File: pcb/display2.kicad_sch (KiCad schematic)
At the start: 35 parts, among them Q13 2N7002K, Q14 2N7002K, Q15 2N7002K, Q16 2N7002K, Q17 BSS84, Q18 BSS84, Q19 BSS84, Q20 BSS84, Q21 BSS84, Q22 BSS84, Q23 BSS84, Q24 BSS84, U3 74HC595

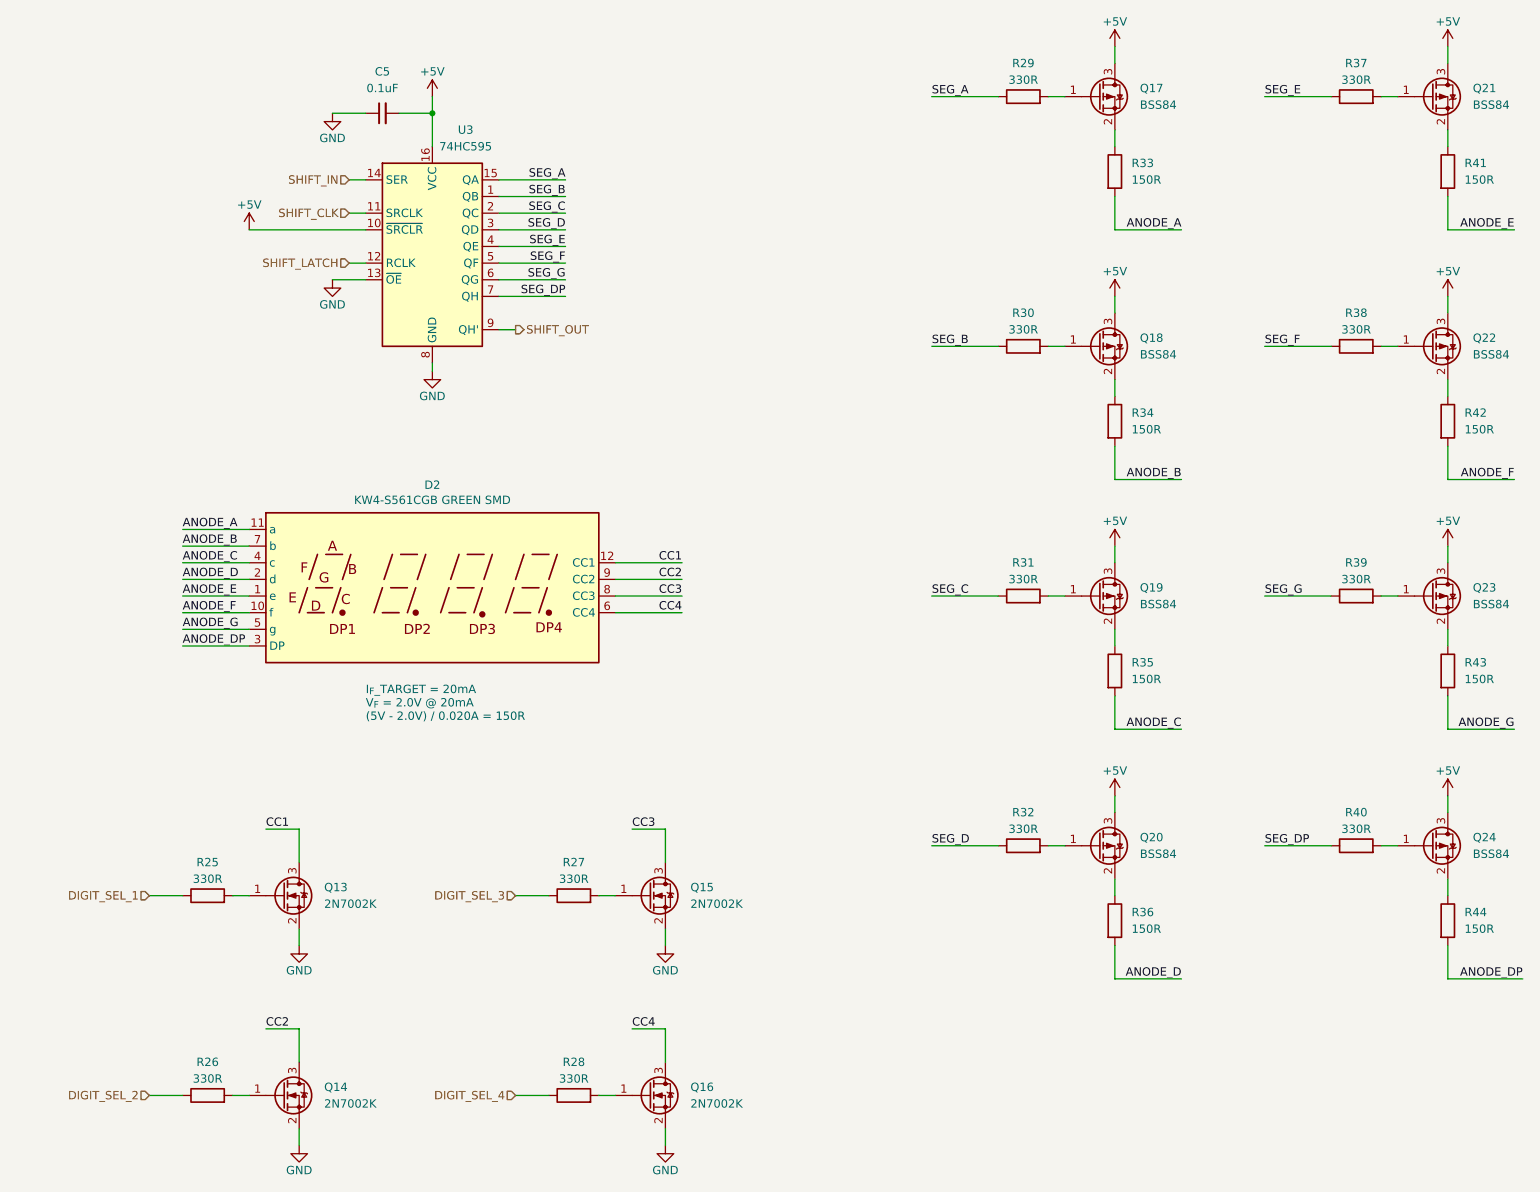
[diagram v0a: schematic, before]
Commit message: tentative schematic for common cathode
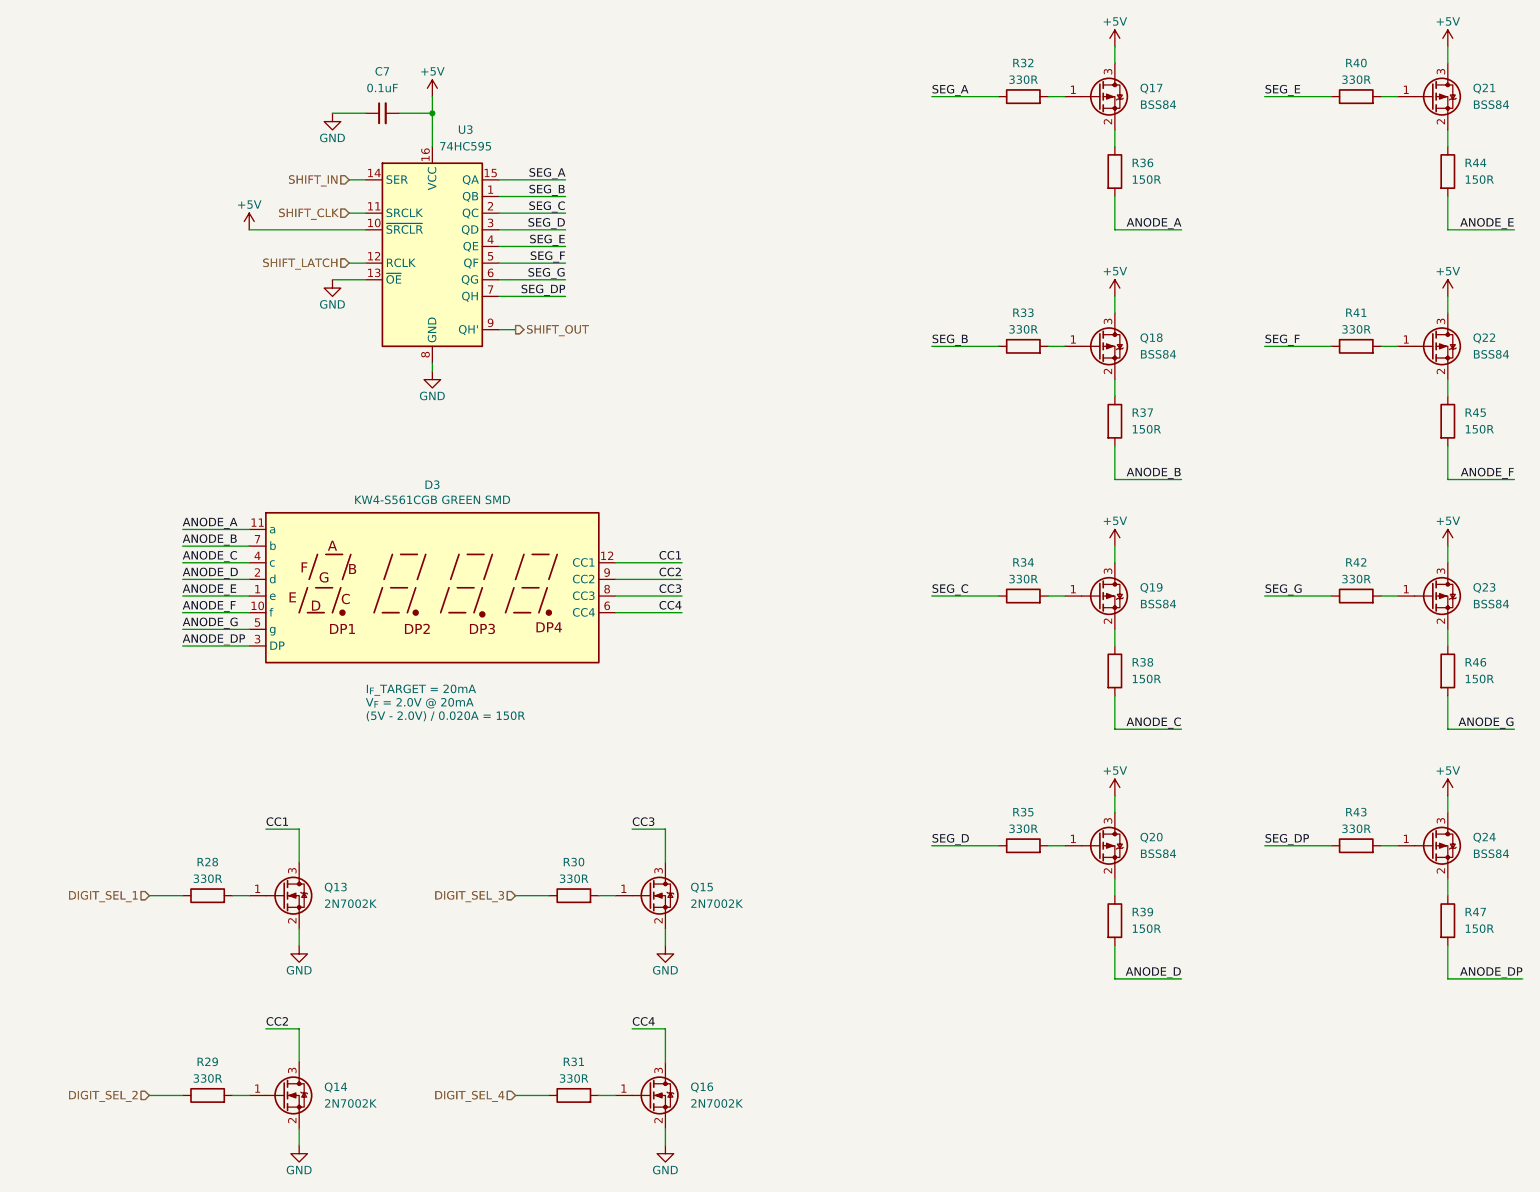
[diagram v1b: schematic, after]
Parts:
- C7: renamed from C5; footprint (none) -> Capacitor_SMD:C_0805_2012Metric_Pad1.18x1.45mm_HandSolder
- R28: renamed from R25; footprint Resistor_SMD:R_0805_2012Metric_Pad1.15x1.40mm_HandSolder -> Resistor_SMD:R_0805_2012Metric_Pad1.20x1.40mm_HandSolder
- R29: renamed from R26; footprint Resistor_SMD:R_0805_2012Metric_Pad1.15x1.40mm_HandSolder -> Resistor_SMD:R_0805_2012Metric_Pad1.20x1.40mm_HandSolder
- R30: renamed from R27; footprint Resistor_SMD:R_0805_2012Metric_Pad1.15x1.40mm_HandSolder -> Resistor_SMD:R_0805_2012Metric_Pad1.20x1.40mm_HandSolder
- R31: renamed from R28; footprint Resistor_SMD:R_0805_2012Metric_Pad1.15x1.40mm_HandSolder -> Resistor_SMD:R_0805_2012Metric_Pad1.20x1.40mm_HandSolder
- R32: renamed from R29; footprint Resistor_SMD:R_0805_2012Metric_Pad1.15x1.40mm_HandSolder -> Resistor_SMD:R_0805_2012Metric_Pad1.20x1.40mm_HandSolder
- R33: renamed from R30; footprint Resistor_SMD:R_0805_2012Metric_Pad1.15x1.40mm_HandSolder -> Resistor_SMD:R_0805_2012Metric_Pad1.20x1.40mm_HandSolder
- R34: renamed from R31; footprint Resistor_SMD:R_0805_2012Metric_Pad1.15x1.40mm_HandSolder -> Resistor_SMD:R_0805_2012Metric_Pad1.20x1.40mm_HandSolder
- R35: renamed from R32; footprint Resistor_SMD:R_0805_2012Metric_Pad1.15x1.40mm_HandSolder -> Resistor_SMD:R_0805_2012Metric_Pad1.20x1.40mm_HandSolder
- R36: renamed from R33; footprint (none) -> Resistor_SMD:R_0805_2012Metric_Pad1.20x1.40mm_HandSolder
- R37: renamed from R34; footprint (none) -> Resistor_SMD:R_0805_2012Metric_Pad1.20x1.40mm_HandSolder
- R38: renamed from R35; footprint (none) -> Resistor_SMD:R_0805_2012Metric_Pad1.20x1.40mm_HandSolder
- R39: renamed from R36; footprint (none) -> Resistor_SMD:R_0805_2012Metric_Pad1.20x1.40mm_HandSolder
- R40: renamed from R37; footprint Resistor_SMD:R_0805_2012Metric_Pad1.15x1.40mm_HandSolder -> Resistor_SMD:R_0805_2012Metric_Pad1.20x1.40mm_HandSolder
- R41: renamed from R38; footprint Resistor_SMD:R_0805_2012Metric_Pad1.15x1.40mm_HandSolder -> Resistor_SMD:R_0805_2012Metric_Pad1.20x1.40mm_HandSolder
- R42: renamed from R39; footprint Resistor_SMD:R_0805_2012Metric_Pad1.15x1.40mm_HandSolder -> Resistor_SMD:R_0805_2012Metric_Pad1.20x1.40mm_HandSolder
- R43: renamed from R40; footprint Resistor_SMD:R_0805_2012Metric_Pad1.15x1.40mm_HandSolder -> Resistor_SMD:R_0805_2012Metric_Pad1.20x1.40mm_HandSolder
- R44: renamed from R41; footprint (none) -> Resistor_SMD:R_0805_2012Metric_Pad1.20x1.40mm_HandSolder
- R45: renamed from R42; footprint (none) -> Resistor_SMD:R_0805_2012Metric_Pad1.20x1.40mm_HandSolder
- R46: renamed from R43; footprint (none) -> Resistor_SMD:R_0805_2012Metric_Pad1.20x1.40mm_HandSolder
- R47: renamed from R44; footprint (none) -> Resistor_SMD:R_0805_2012Metric_Pad1.20x1.40mm_HandSolder
- renumbered D2 to D3

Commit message: common anode schematic
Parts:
- removed C7: 0.1uF, Capacitor_SMD:C_0805_2012Metric_Pad1.18x1.45mm_HandSolder, symbol Device:C_Small
- removed D3: KW4-S561CGB GREEN SMD, mtg_life_counter:KW4-S561xxB_SMD, symbol mtg_life_counter:KW4-S561CxB
- removed Q13, Q14, Q15, Q16: 2N7002K, Package_TO_SOT_SMD:SOT-23, symbol Transistor_FET:2N7002K
- removed Q17, Q18, Q19, Q20, Q21, Q22, Q23, Q24: BSS84, Package_TO_SOT_SMD:SOT-23, symbol Transistor_FET:BSS84
- removed R34, R35, R40, R41, R42, R43: 330R, Resistor_SMD:R_0805_2012Metric_Pad1.20x1.40mm_HandSolder, symbol Device:R
- removed R36, R37, R38, R39, R44, R45, R46, R47: 150R, Resistor_SMD:R_0805_2012Metric_Pad1.20x1.40mm_HandSolder, symbol Device:R
- removed U3: 74HC595, Package_SO:SOIC-16_3.9x9.9mm_P1.27mm, symbol 74xx:74HC595
- added D3: KW4-S561AGB, mtg_life_counter:KW4-S561xxB_SMD, symbol mtg_life_counter:KW4-S561AxB
- added Q5, Q6, Q7, Q8: DMG2301L, Package_TO_SOT_SMD:SOT-23, symbol Transistor_FET:DMG2301L
- added R21, R22, R23, R24: 330R, Resistor_SMD:R_0805_2012Metric_Pad1.20x1.40mm_HandSolder, symbol Device:R
- added R25, R26, R27: 150R, Resistor_SMD:R_0805_2012Metric_Pad1.20x1.40mm_HandSolder, symbol Device:R
- added U3: TPIC6C596, Package_SO:SOIC-16_3.9x9.9mm_P1.27mm, symbol mtg_life_counter:TPIC6C596
- R28, R29, R30, R31, R32: value 330R -> 150R
- R33: value 330R -> 10k
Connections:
- net SEG_B is gone; now on net +5V: R33.1
- net +5V: now also Q5.3 (D), Q6.3 (D), Q7.3 (D), Q8.3 (D), U3.1 (VCC)
- net DIGIT_SEL_1: now also R21.1; no longer R28.1
- net DIGIT_SEL_2: now also R22.1; no longer R29.1
- net DIGIT_SEL_3: now also R23.1; no longer R30.1
- net DIGIT_SEL_4: now also R24.1; no longer R31.1
- net GND: now also U3.16 (GND), U3.8 (~{G})
- net SHIFT_CLK: now also U3.15 (SRCK)
- net SHIFT_IN: now also U3.2 (SER_IN)
- net SHIFT_LATCH: now also U3.10 (RCLK)
- net SHIFT_OUT: now also U3.9 (SER_OUT)
- net at R33.2: now also U3.7 (~{SRCLR})
- net SF: now reaches R30.2
- net SF: now also U3.12 (DRAIN5)
- net SE: now reaches R29.2
- net SE: now also U3.11 (DRAIN4)
- net SD: now reaches R28.2
- net SD: now also U3.6 (DRAIN3)
- net SG: now reaches R31.2
- net SG: now also U3.13 (DRAIN6)
- net SDP: now reaches R32.2
- net SDP: now also U3.14 (DRAIN7)
- net SEG_A renamed ADP
- net ADP: now also D3.3 (DP)
- new net: Q7.1 (G), R23.2
- new net: Q8.1 (G), R24.2
- new net: Q5.1 (G), R21.2
- new net: Q6.1 (G), R22.2
- new net AA: D3.11 (a), R25.1
- new net AB: D3.7 (b), R26.1
- new net AC: D3.4 (c), R27.1
- new net AD: D3.2 (d), R28.1
- new net AE: D3.1 (e), R29.1
- new net AF: D3.10 (f), R30.1
- new net AG: D3.5 (g), R31.1
- new net CA1: D3.12 (CA1), Q5.2 (S)
- new net CA2: D3.9 (CA2), Q6.2 (S)
- new net CA3: D3.8 (CA3), Q7.2 (S)
- new net CA4: D3.6 (CA4), Q8.2 (S)
- new net SA: R25.2, U3.3 (DRAIN0)
- new net SB: R26.2, U3.4 (DRAIN1)
- new net SC: R27.2, U3.5 (DRAIN2)

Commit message: continue wip
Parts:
- added C6: 0.1uF, Capacitor_SMD:C_0805_2012Metric_Pad1.18x1.45mm_HandSolder, symbol Device:C_Small
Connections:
- net +5V: now also C6.1
- net GND: now also C6.2
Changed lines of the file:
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@@
+	(wire
+		(pts
+			(xy 198.12 48.26) (xy 198.12 50.8)
+		)
+		(stroke
+			(width 0)
+			(type default)
+		)
+	)
 	(wire
 		(pts
@@
 		(pts
 			(xy 63.5 73.66) (xy 90.17 73.66)
+		)
+		(stroke
+			(width 0)
+			(type default)
+		)
+	)
+	(wire
+		(pts
+			(xy 198.12 55.88) (xy 198.12 58.42)
 		)
 		(stroke
@@
 	)
 	(symbol
+		(lib_id "power:GND")
+		(at 198.12 58.42 0)
+		(unit 1)
+		(exclude_from_sim no)
+		(in_bom yes)
+		(on_board yes)
+		(dnp no)
+		(property "Reference" "#PWR063"
+			(at 198.12 64.77 0)
+			(effects
+				(font
+					(size 1.27 1.27)
+				)
+				(hide yes)
+			)
+		)
+		(property "Value" "GND"
+			(at 198.12 62.23 0)
+			(effects
+				(font
+					(size 1.27 1.27)
+				)
+			)
+		)
+		(property "Footprint" ""
+			(at 198.12 58.42 0)
+			(effects
+				(font
+					(size 1.27 1.27)
+				)
+				(hide yes)
+			)
+		)
+		(property "Datasheet" ""
+			(at 198.12 58.42 0)
+			(effects
+				(font
+					(size 1.27 1.27)
+				)
+				(hide yes)
+			)
+		)
+		(property "Description" "Power symbol creates a global label with name \"GND\" , ground"
+			(at 198.12 58.42 0)
+			(effects
+				(font
+					(size 1.27 1.27)
+				)
+				(hide yes)
+			)
+		)
+		(pin "1"
+		)
+		(instances
+			(project "mtg_life_counter"
+				(path "/1883df74-0bd5-446c-9076-f848bb3cfebf/071d9a1a-c1d1-4831-ad0b-9d7b579fcd0c"
+					(reference "#PWR063")
+					(unit 1)
+				)
+			)
+		)
+	)
+	(symbol
 		(lib_id "mtg_life_counter-rescue:+5V-power")
 		(at 63.5 86.36 0)
@@
 	)
 	(symbol
+		(lib_id "power:+5V")
+		(at 198.12 48.26 0)
+		(unit 1)
+		(exclude_from_sim no)
+		(in_bom yes)
+		(on_board yes)
+		(dnp no)
+		(property "Reference" "#PWR064"
+			(at 198.12 52.07 0)
+			(effects
+				(font
+					(size 1.27 1.27)
+				)
+				(hide yes)
+			)
+		)
+		(property "Value" "+5V"
+			(at 198.12 44.45 0)
+			(effects
+				(font
+					(size 1.27 1.27)
+				)
+			)
+		)
+		(property "Footprint" ""
+			(at 198.12 48.26 0)
+			(effects
+				(font
+					(size 1.27 1.27)
+				)
+				(hide yes)
+			)
+		)
+		(property "Datasheet" ""
+			(at 198.12 48.26 0)
+			(effects
+				(font
+					(size 1.27 1.27)
+				)
+				(hide yes)
+			)
+		)
+		(property "Description" "Power symbol creates a global label with name \"+5V\""
+			(at 198.12 48.26 0)
+			(effects
+				(font
+					(size 1.27 1.27)
+				)
+				(hide yes)
+			)
+		)
+		(pin "1"
+		)
+		(instances
+			(project "mtg_life_counter"
+				(path "/1883df74-0bd5-446c-9076-f848bb3cfebf/071d9a1a-c1d1-4831-ad0b-9d7b579fcd0c"
+					(reference "#PWR064")
+					(unit 1)
+				)
+			)
+		)
+	)
+	(symbol
 		(lib_id "mtg_life_counter-rescue:+5V-power")
 		(at 63.5 55.88 0)
@@
 					(unit 1)
 				)
+			)
+		)
+	)
+	(symbol
+		(lib_id "Device:C_Small")
+		(at 198.12 53.34 0)
+		(mirror y)
+		(unit 1)
+		(exclude_from_sim no)
+		(in_bom yes)
+		(on_board yes)
+		(dnp no)
+		(fields_autoplaced yes)
+		(property "Reference" "C6"
+			(at 200.66 52.0762 0)
+			(effects
+				(font
+					(size 1.27 1.27)
+				)
+				(justify right)
+			)
+		)
+		(property "Value" "0.1uF"
+			(at 200.66 54.6162 0)
+			(effects
+				(font
+					(size 1.27 1.27)
+				)
+				(justify right)
+			)
+		)
+		(property "Footprint" "Capacitor_SMD:C_0805_2012Metric_Pad1.18x1.45mm_HandSolder"
+			(at 198.12 53.34 0)
+			(effects
+				(font
+					(size 1.27 1.27)
+				)
+				(hide yes)
+			)
+		)
+		(property "Datasheet" "~"
+			(at 198.12 53.34 0)
+			(effects
+				(font
+					(size 1.27 1.27)
+				)
+				(hide yes)
+			)
+		)
+		(property "Description" "Unpolarized capacitor, small symbol"
+			(at 198.12 53.34 0)
+			(effects
+				(font
+					(size 1.27 1.27)
+				)
+				(hide yes)
+			)
+		)
+		(pin "2"
+		)
+		(pin "1"
+		)
+		(instances
+			(project ""
+				(path "/1883df74-0bd5-446c-9076-f848bb3cfebf/071d9a1a-c1d1-4831-ad0b-9d7b579fcd0c"
+					(reference "C6")
+					(unit 1)
+				)
